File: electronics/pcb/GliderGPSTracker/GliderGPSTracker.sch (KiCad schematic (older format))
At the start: 16 parts

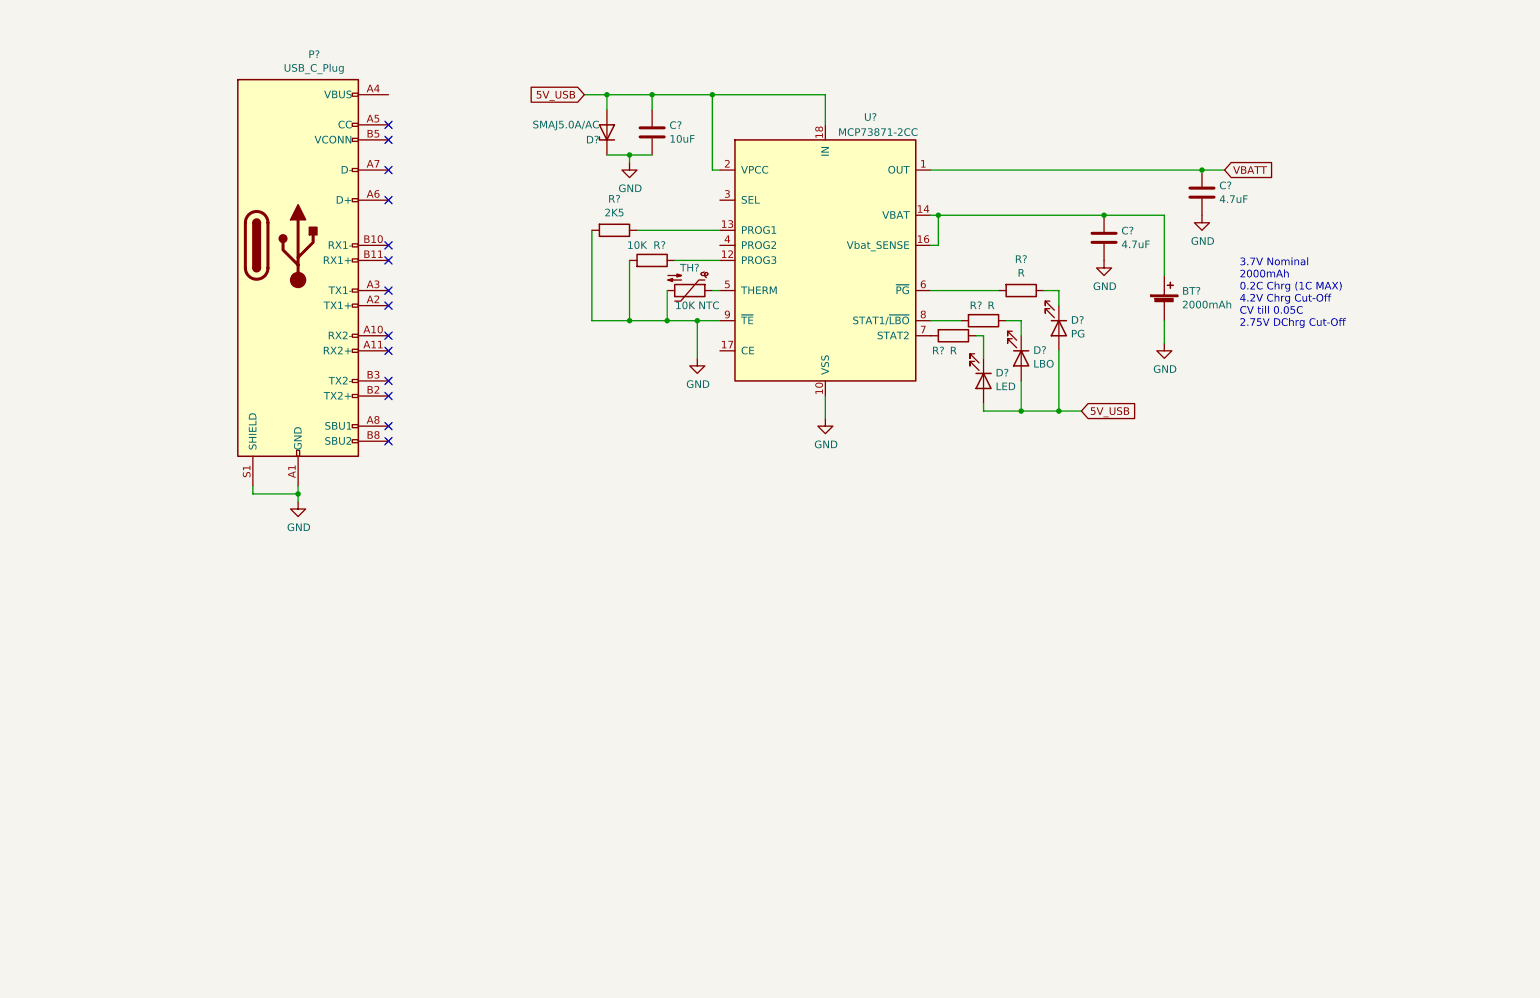
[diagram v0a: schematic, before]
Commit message: Task: Refine battery circuitry
The battery charging and proteciton circuitry has been largely
completed. A USB-C connector has been added and the microcontroller
will be responsible for recognising the charging source, hence the
limit on the max avaiable current draw for charging.
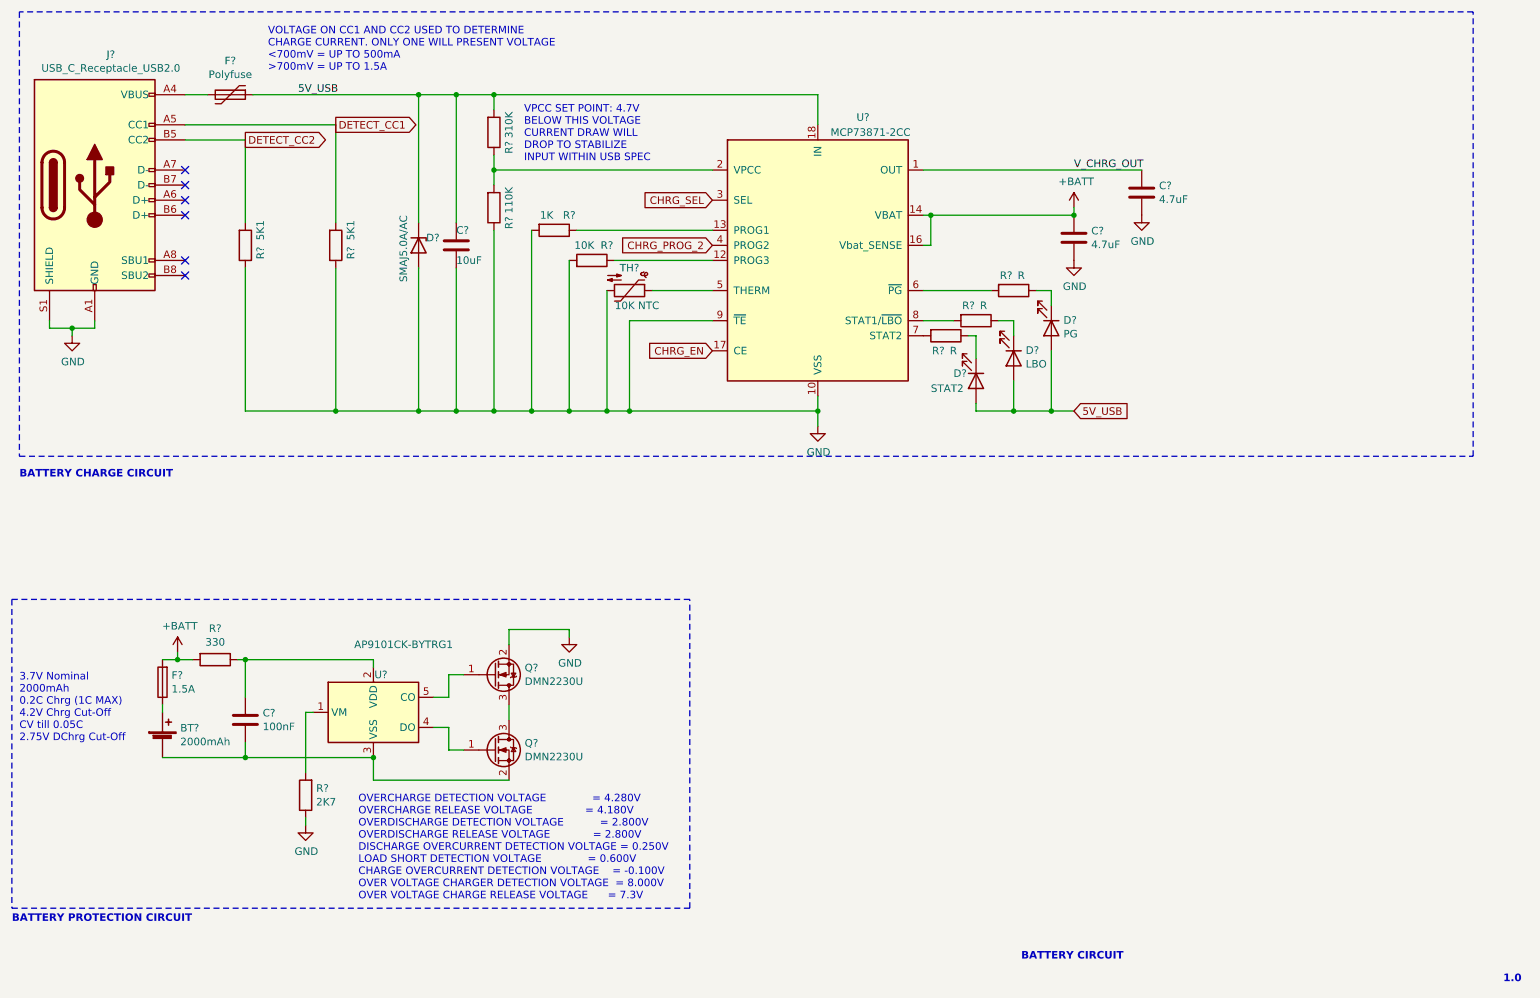
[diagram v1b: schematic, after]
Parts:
- removed P?: USB_C_Plug, symbol Connector:USB_C_Plug
- added C?: 100nF, symbol Device:C
- added F?: Polyfuse, symbol Device:Polyfuse
- added F?: 1.5A, symbol Device:Fuse
- added J?: USB_C_Receptacle_USB2.0, symbol Connector:USB_C_Receptacle_USB2.0
- added Q? (x2): DMN2230U, Package_TO_SOT_SMD:SOT-23, symbol Transistor_FET:DMN2230U
- added R?: 310K, symbol Device:R
- added R?: 110K, symbol Device:R
- added R? (x2): 5K1, symbol Device:R
- added R?: 330, symbol Device:R
- added R?: 2K7, symbol Device:R
- added U?: AP9101CK-BYTRG1, Package_TO_SOT_SMD:SOT-23-5, symbol Battery_Management:AP9101CK
- D?: value LED -> STAT2
- R?: value 2K5 -> 1K
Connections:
- net 5V_USB: now also D?.1 (K), F?.1, R?.2; no longer D?.2 (A), U?.2 (VPCC)
- net GND: now also D?.2 (A), J?.A1 (GND), J?.A12 (GND), J?.B1 (GND), J?.B12 (GND), J?.S1 (SHIELD), Q?.2 (S), R?.1, R?.1, R?.1, R?.1; no longer BT?.2 (-), D?.1 (K)
- net +BATT: now reaches C?.1, U?.14 (VBAT), U?.15 (VBAT), U?.16 (Vbat_SENSE)
- net +BATT: now also F?.2, R?.2; no longer BT?.1 (+)
- net CHRG_EN: now reaches U?.17 (CE)
- net CHRG_SEL: now reaches U?.3 (SEL)
- net CHRG_PROG_2: now reaches U?.4 (PROG2)
- net VBATT renamed V_CHRG_OUT
- new net: R?.1, R?.2, U?.2 (VPCC)
- new net: BT?.1 (+), F?.1
- new net: BT?.2 (-), C?.2, Q?.2 (S), U?.3 (VSS)
- new net: F?.2, J?.A4 (VBUS), J?.A9 (VBUS), J?.B4 (VBUS), J?.B9 (VBUS)
- new net: R?.2, U?.1 (VM)
- new net: C?.1, R?.1, U?.2 (VDD)
- new net: Q?.1 (G), U?.4 (DO)
- new net: Q?.1 (G), U?.5 (CO)
- new net: Q?.3 (D), Q?.3 (D)
- new net DETECT_CC1: J?.A5 (CC1), R?.2
- new net DETECT_CC2: J?.B5 (CC2), R?.2
- no-connect marks 14 -> 6
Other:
- note added: "1.0"
- note added: "BATTERY CHARGE CIRCUIT"
- note added: "BATTERY CIRCUIT"
- note added: "BATTERY PROTECTION CIRCUIT"
- note added: "OVERCHARGE DETECTION VOLTAGE = 4.280V\nOVERCHARGE RELEASE VOLTAGE = 4.180V\nOVERDISCHARGE DETECTION VOLTAGE = 2.800V\nOVERDISCHARGE RELEASE VOLTAGE = 2.800V\nDISCHARGE OVERCURRENT DETECTION VOLTAGE = 0.250V\nLOAD SHORT DETECTION VOLTAGE = 0.600V\nCHARGE OVERCURRENT DETECTION VOLTAGE = -0.100V\nOVER VOLTAGE CHARGER DETECTION VOLTAGE = 8.000V\nOVER VOLTAGE CHARGE RELEASE VOLTAGE = 7.3V"
- note added: "VOLTAGE ON CC1 AND CC2 USED TO DETERMINE\nCHARGE CURRENT. ONLY ONE WILL PRESENT VOLTAGE\n<700mV = UP TO 500mA\n>700mV = UP TO 1.5A"
- note added: "VPCC SET POINT: 4.7V\nBELOW THIS VOLTAGE\nCURRENT DRAW WILL\nDROP TO STABILIZE\nINPUT WITHIN USB SPEC"
- moved on the sheet: BT?, C?, D?, R?, TH?, U?

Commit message: Task: Split schematic into blocks
The power oriented blocks have been split into their own schematic
pages within kicad
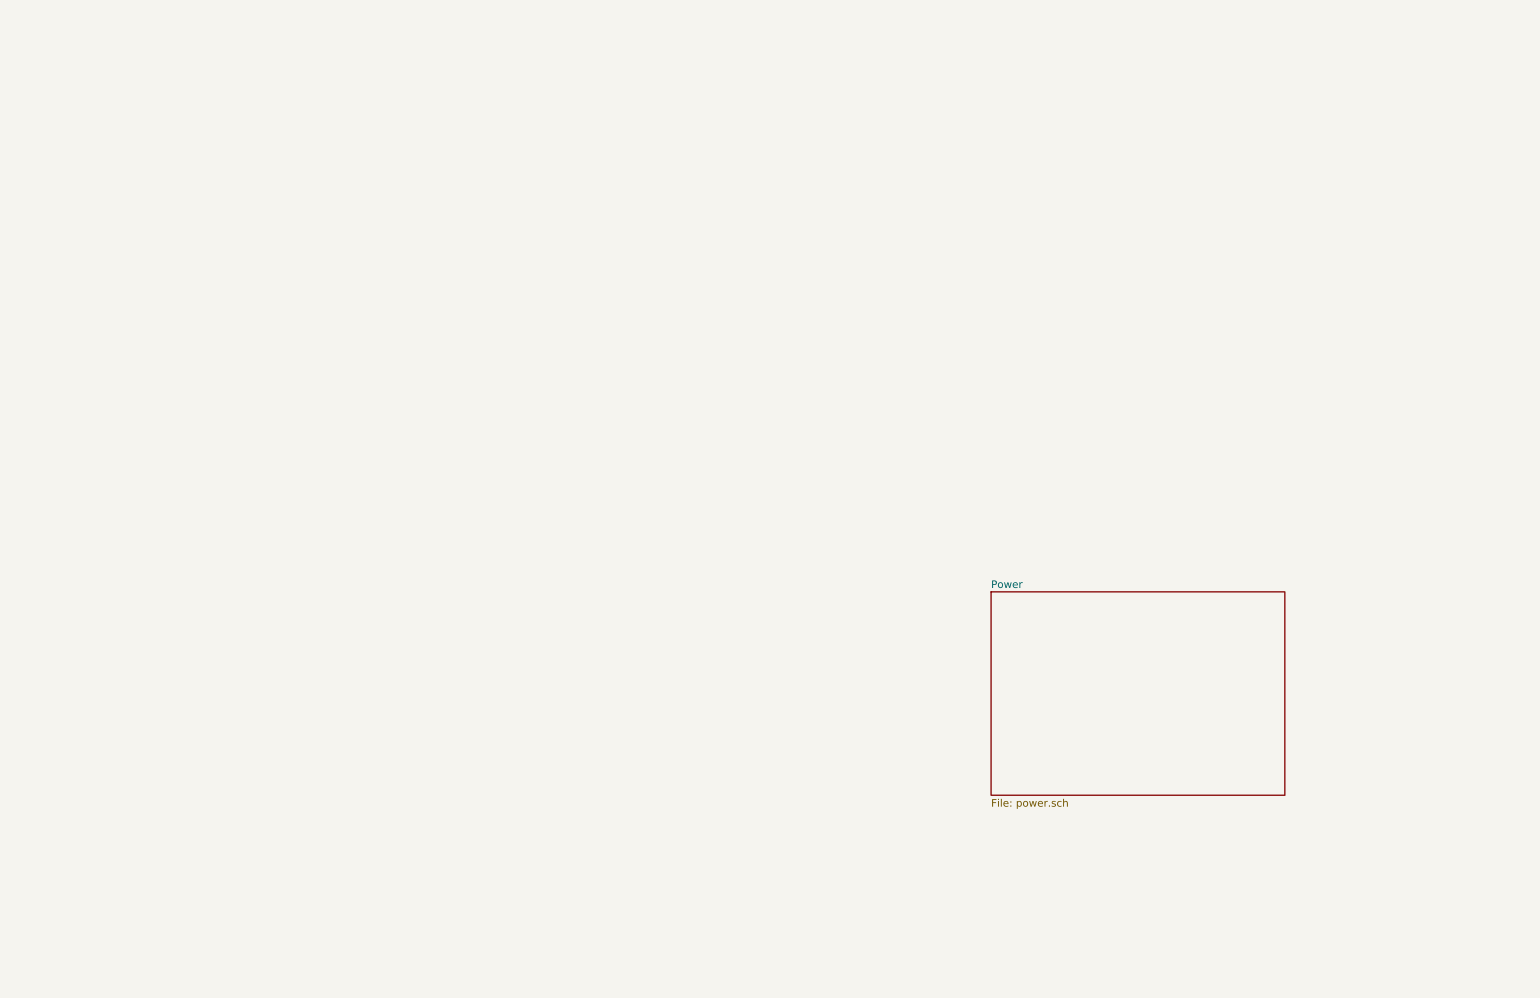
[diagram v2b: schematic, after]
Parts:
- removed BT?: 2000mAh, symbol Device:Battery_Cell
- removed C? (x2): 4.7uF, symbol Device:C
- removed C?: 10uF, symbol Device:C
- removed C?: 100nF, symbol Device:C
- removed D?: PG, symbol Device:LED
- removed D?: LBO, symbol Device:LED
- removed D?: STAT2, symbol Device:LED
- removed D?: SMAJ5.0A/AC, symbol Device:D_Zener
- removed F?: Polyfuse, symbol Device:Polyfuse
- removed F?: 1.5A, symbol Device:Fuse
- removed J?: USB_C_Receptacle_USB2.0, symbol Connector:USB_C_Receptacle_USB2.0
- removed Q? (x2): DMN2230U, Package_TO_SOT_SMD:SOT-23, symbol Transistor_FET:DMN2230U
- removed R? (x3): R, symbol Device:R
- removed R?: 1K, symbol Device:R
- removed R?: 10K, symbol Device:R
- removed R?: 310K, symbol Device:R
- removed R?: 110K, symbol Device:R
- removed R? (x2): 5K1, symbol Device:R
- removed R?: 330, symbol Device:R
- removed R?: 2K7, symbol Device:R
- removed TH?: 10K NTC, symbol Device:Thermistor_NTC
- removed U?: MCP73871-2CC, Package_DFN_QFN:QFN-20-1EP_4x4mm_P0.5mm_EP2.5x2.5mm, symbol Battery_Management:MCP73871-2CC
- removed U?: AP9101CK-BYTRG1, Package_TO_SOT_SMD:SOT-23-5, symbol Battery_Management:AP9101CK
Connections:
- no-connect marks 6 -> 0
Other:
- note removed: "1.0"
- note removed: "3.7V Nominal\n2000mAh\n0.2C Chrg (1C MAX)\n4.2V Chrg Cut-Off\nCV till 0.05C\n2.75V DChrg Cut-Off\n"
- note removed: "BATTERY CHARGE CIRCUIT"
- note removed: "BATTERY CIRCUIT"
- note removed: "BATTERY PROTECTION CIRCUIT"
- note removed: "OVERCHARGE DETECTION VOLTAGE = 4.280V\nOVERCHARGE RELEASE VOLTAGE = 4.180V\nOVERDISCHARGE DETECTION VOLTAGE = 2.800V\nOVERDISCHARGE RELEASE VOLTAGE = 2.800V\nDISCHARGE OVERCURRENT DETECTION VOLTAGE = 0.250V\nLOAD SHORT DETECTION VOLTAGE = 0.600V\nCHARGE OVERCURRENT DETECTION VOLTAGE = -0.100V\nOVER VOLTAGE CHARGER DETECTION VOLTAGE = 8.000V\nOVER VOLTAGE CHARGE RELEASE VOLTAGE = 7.3V"
- note removed: "VOLTAGE ON CC1 AND CC2 USED TO DETERMINE\nCHARGE CURRENT. ONLY ONE WILL PRESENT VOLTAGE\n<700mV = UP TO 500mA\n>700mV = UP TO 1.5A"
- note removed: "VPCC SET POINT: 4.7V\nBELOW THIS VOLTAGE\nCURRENT DRAW WILL\nDROP TO STABILIZE\nINPUT WITHIN USB SPEC"

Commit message: Task: Begin SIM7000E implementation
Work has begun on adding the SIM7000E module to the schematic.
A schematic symbol and footprint have been made to this end.
The basic SIM card circuit and power circuit has been set up
which include ESD protection IC's.
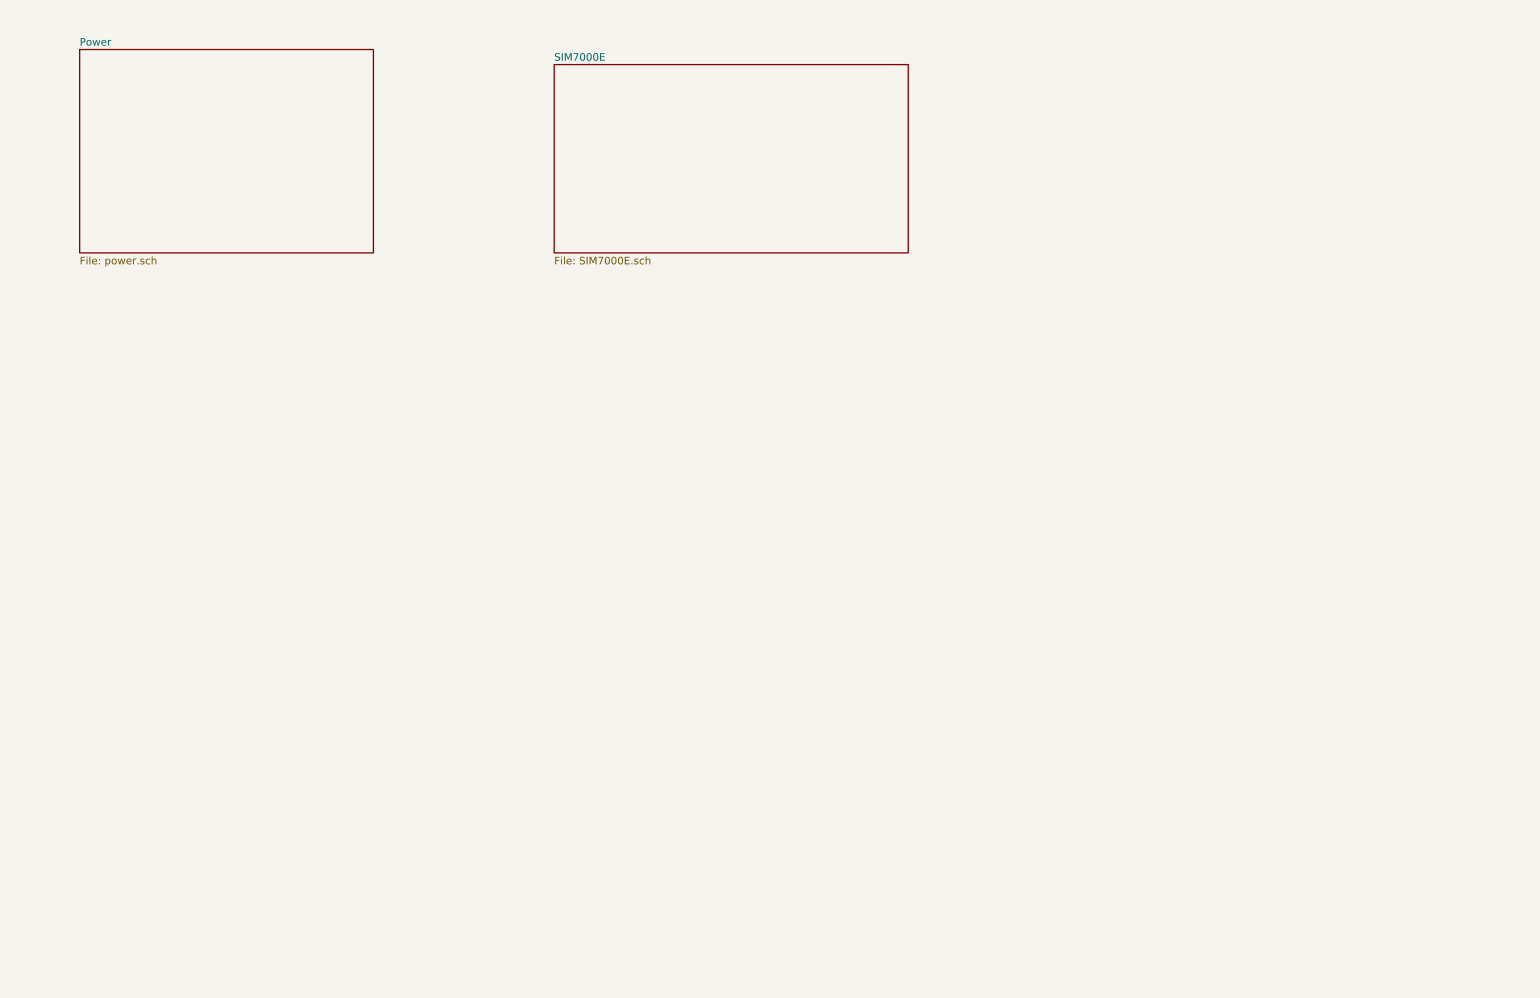
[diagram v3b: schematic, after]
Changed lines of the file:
@@
 $Descr A4 11693 8268
 encoding utf-8
-Sheet 1 2
-Title ""
+Sheet 1 3
+Title "GLIDER GPS TRACKER"
 Date ""
-Rev ""
+Rev "1.0"
 Comp ""
 Comment1 ""
@@
 $EndDescr
 $Sheet
-S 7200 5050 1950 1350
+S 1150 1450 1950 1350
 U 6090E0C9
 F0 "Power" 50
 F1 "power.sch" 50
 $EndSheet
+$Sheet
+S 4300 1550 2350 1250
+U 608FF5E2
+F0 "SIM7000E" 50
+F1 "SIM7000E.sch" 50
+$EndSheet
 $EndSCHEMATC

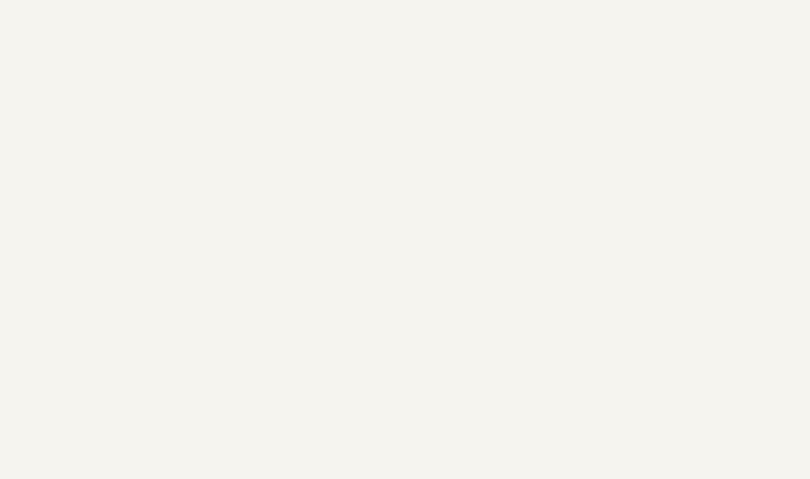
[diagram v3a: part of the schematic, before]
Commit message: Task: SIM7000 Powerkey, reset, USB, UART implementation
The SIM7000 schematic has been updated to include the recommended
layouts for the Powerkey pin, reset pin, USB and UART buses, and
netlight pin. The usb connector in the power schematic has also
been updated to accomodate the additions.
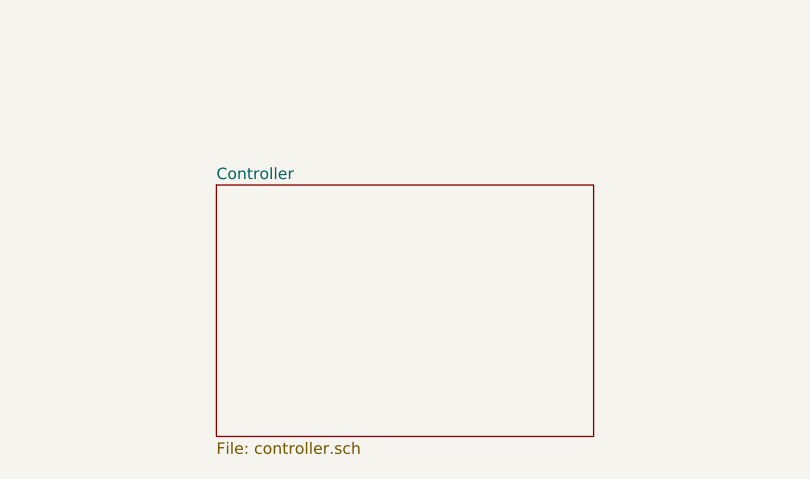
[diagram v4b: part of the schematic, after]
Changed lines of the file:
@@
 $Descr A4 11693 8268
 encoding utf-8
-Sheet 1 3
+Sheet 1 4
 Title "GLIDER GPS TRACKER"
 Date ""
@@
 F1 "SIM7000E.sch" 50
 $EndSheet
+$Sheet
+S 2700 4100 1650 1100
+U 60CDF4B0
+F0 "Controller" 50
+F1 "controller.sch" 50
+$EndSheet
 $EndSCHEMATC
